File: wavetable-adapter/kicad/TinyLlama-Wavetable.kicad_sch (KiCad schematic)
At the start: 11 parts, among them J1 TINYLLAMA_PI_CONN, J2 PI_ZERO, J3 WAVETABLE, J4 AUDIO_OUT, J5 P_CONN_01X03, J6 P_CONN_01x06, SW1 PI_WT_TOGGLE

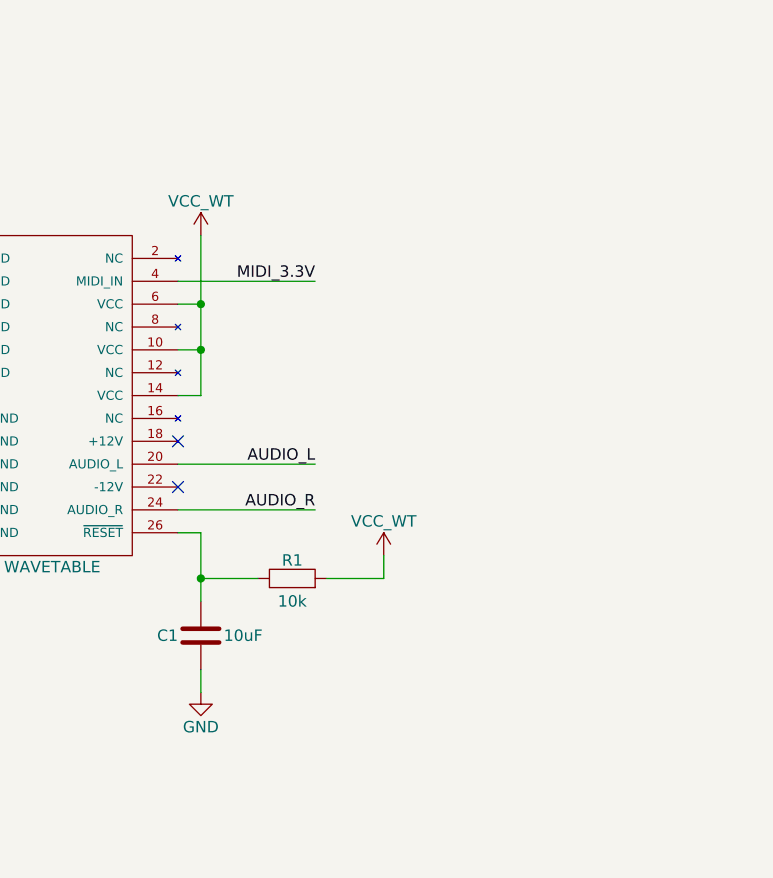
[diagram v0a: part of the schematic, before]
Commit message: Add files via upload
updated schematic to add +/-12 DC2DC and 3v3 to 5v level shifter.
PCB and footprint for PDME2-S5-D12 is still remaining
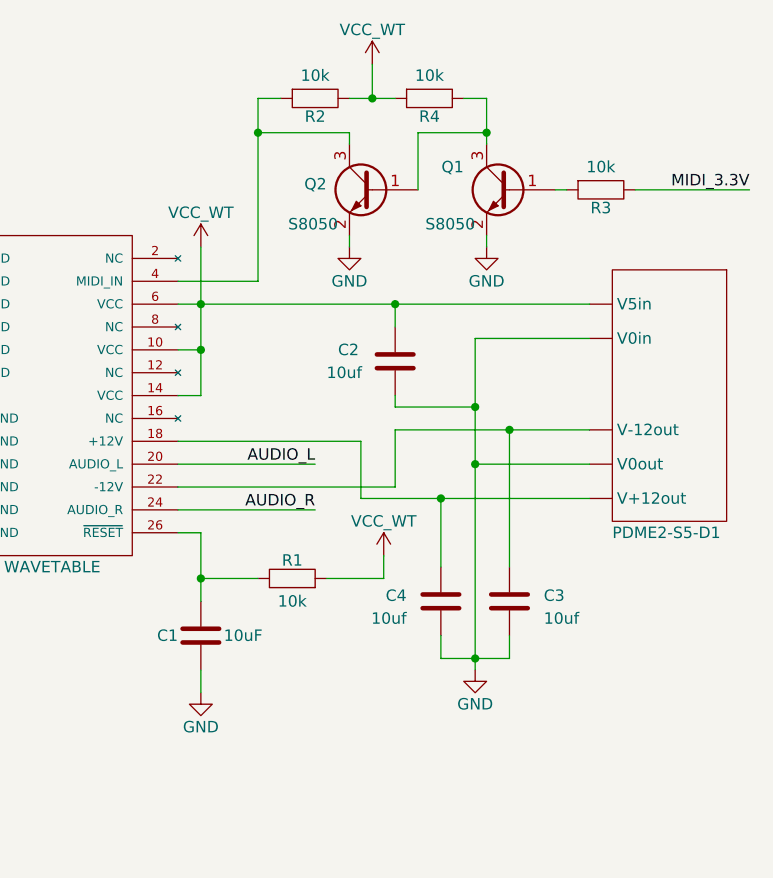
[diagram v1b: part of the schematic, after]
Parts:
- added C2, C3, C4: 10uf, Capacitor_SMD:C_0805_2012Metric, symbol Device:C
- added PDME2-S5-D1: ~, symbol PDME:PDME2-S5-D12
- added Q1: S8050, Package_TO_SOT_THT:TO-92_Inline, symbol Transistor_BJT:S8050
- added Q2: S8050, Package_TO_SOT_SMD:SOT-23, symbol Transistor_BJT:S8050
- added R2, R3, R4: 10k, Resistor_SMD:R_0603_1608Metric, symbol llama_shared:R
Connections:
- net GND: now also C2.2, C3.2, C4.2, PDME2-S5-D1. (V5in), Q1.2 (E), Q2.2 (E)
- net MIDI_3.3V: now also R3.1; no longer J3.4 (MIDI_IN)
- net VCC_WT: now also C2.1, PDME2-S5-D1. (V5in), R2.1, R4.2
- net at J3.18 (+12V): now also C4.1, PDME2-S5-D1. (V5in)
- net at J3.22 (-12V): now also C3.1, PDME2-S5-D1. (V5in)
- new net: J3.4 (MIDI_IN), Q2.3 (C), R2.2
- new net: Q1.1 (B), R3.2
- new net: Q1.3 (C), Q2.1 (B), R4.1
- no-connect marks 52 -> 50
